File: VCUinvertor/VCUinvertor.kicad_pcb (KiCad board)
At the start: 2 copper layers, 97.3 x 113.8 mm, 96 parts, among them J1 NXP12, J2 NXP11, J3 NXP15, J4 NXP14, J5 NXP10, J6 NXP13, J7 PowerSupply, J8 CAN_NXP, J9 BACKLIGHT, Q1 BSS138, Q10 BSS138, Q2 BSS138, Q3 BSS138, Q4 BSS138, Q5 BSS138, Q6 BSS138, Q7 BSS138, Q8 BSS138, Q9 BSS138, U1 TJA1448ATK, U2 REF3433T, U3 TLV76150DCY

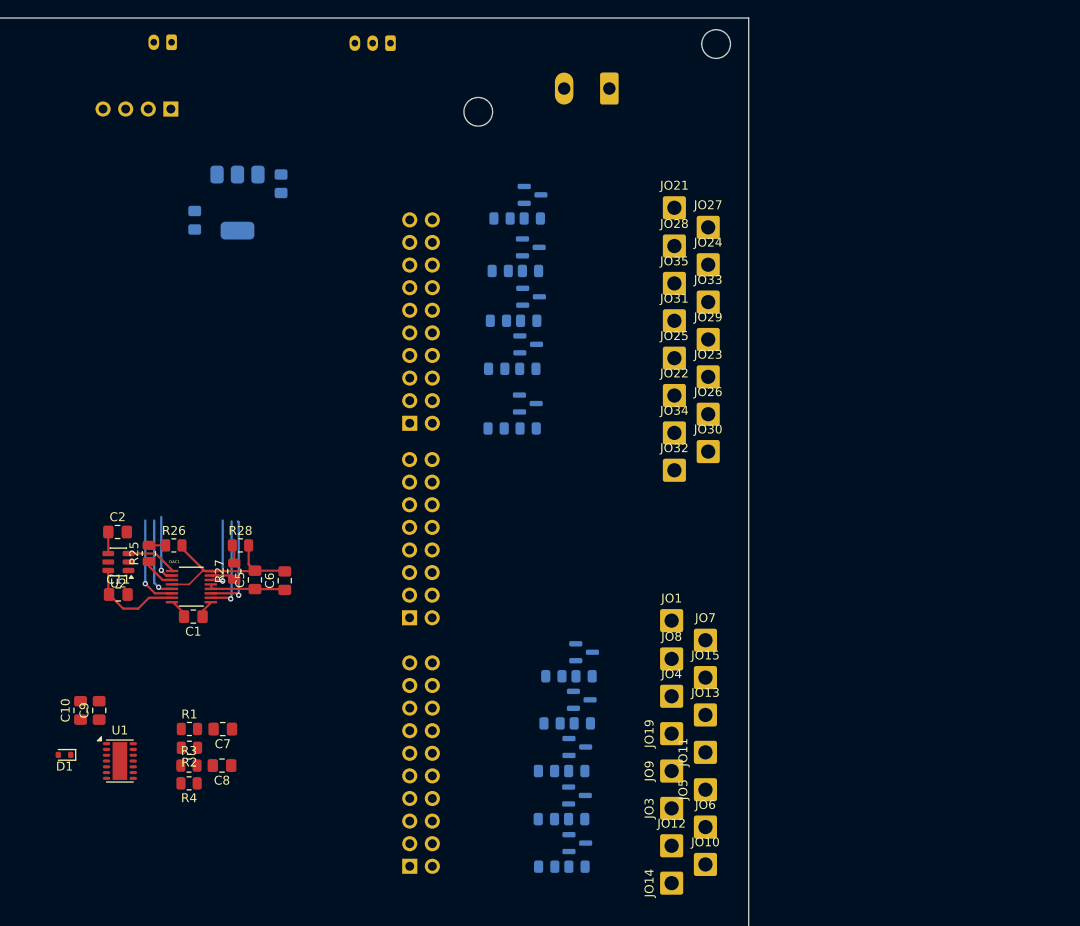
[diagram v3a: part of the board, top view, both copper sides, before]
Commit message: New PMOS config for switching
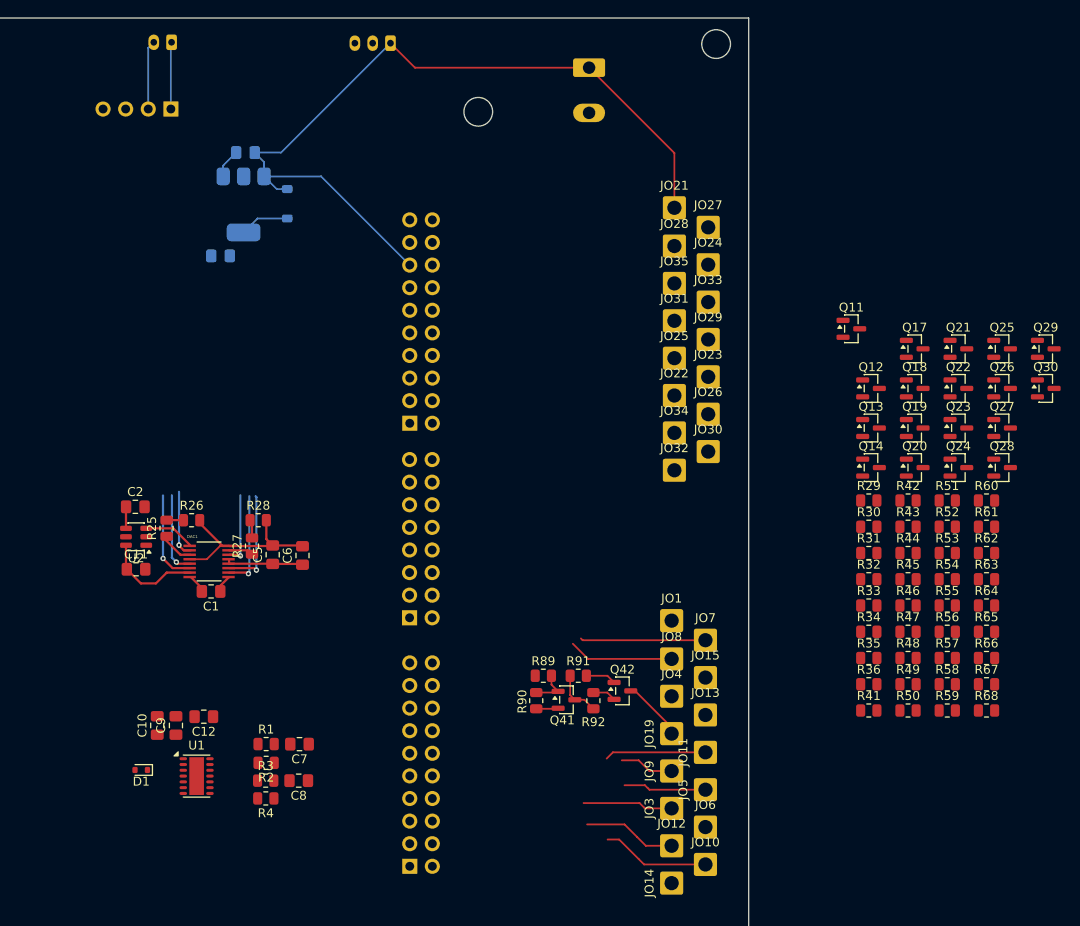
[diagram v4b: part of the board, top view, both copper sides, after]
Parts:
- removed Q1, Q10, Q2, Q3, Q4, Q5, Q6, Q7, Q8, Q9: BSS138, Package_TO_SOT_SMD:SOT-23
- removed R10, R11, R12, R13, R14, R16, R18, R20, R22, R24: 5k, Resistor_SMD:R_0805_2012Metric
- removed R15, R17, R19, R21, R23, R5, R6, R7, R8, R9: 10k, Resistor_SMD:R_0805_2012Metric
- added C12: 0.1uF, Capacitor_SMD:C_0805_2012Metric_Pad1.18x1.45mm_HandSolder, F.Cu at (89.0, 116.3)
- added D1: MBR0540, Diode_SMD:D_SOD-123, B.Cu at (98.4, 58.6)
- added Q11: MMBT3904, Package_TO_SOT_SMD:SOT-23, F.Cu at (161.8, 72.7)
- added Q12: IRLML6402, Package_TO_SOT_SMD:SOT-23, F.Cu at (164.0, 79.4)
- added Q13: MMBT3904, Package_TO_SOT_SMD:SOT-23, F.Cu at (164.0, 83.8)
- added Q14: IRLML6402, Package_TO_SOT_SMD:SOT-23, F.Cu at (164.0, 88.3)
- added Q17: MMBT3904, Package_TO_SOT_SMD:SOT-23, F.Cu at (168.9, 75.0)
- added Q18: MMBT3904, Package_TO_SOT_SMD:SOT-23, F.Cu at (168.9, 79.4)
- added Q19: MMBT3904, Package_TO_SOT_SMD:SOT-23, F.Cu at (168.9, 83.8)
- added Q20: IRLML6402, Package_TO_SOT_SMD:SOT-23, F.Cu at (168.9, 88.3)
- added Q21: IRLML6402, Package_TO_SOT_SMD:SOT-23, F.Cu at (173.8, 75.0)
- added Q22: IRLML6402, Package_TO_SOT_SMD:SOT-23, F.Cu at (173.8, 79.4)
- added Q23: MMBT3904, Package_TO_SOT_SMD:SOT-23, F.Cu at (173.8, 83.8)
- added Q24: IRLML6402, Package_TO_SOT_SMD:SOT-23, F.Cu at (173.8, 88.3)
- added Q25: MMBT3904, Package_TO_SOT_SMD:SOT-23, F.Cu at (178.7, 75.0)
- added Q26: IRLML6402, Package_TO_SOT_SMD:SOT-23, F.Cu at (178.7, 79.4)
- added Q27: MMBT3904, Package_TO_SOT_SMD:SOT-23, F.Cu at (178.7, 83.8)
- added Q28: IRLML6402, Package_TO_SOT_SMD:SOT-23, F.Cu at (178.7, 88.3)
- added Q29: MMBT3904, Package_TO_SOT_SMD:SOT-23, F.Cu at (183.6, 75.0)
- added Q30: IRLML6402, Package_TO_SOT_SMD:SOT-23, F.Cu at (183.6, 79.4)
- added Q41: MMBT3904, Package_TO_SOT_SMD:SOT-23, F.Cu at (129.8, 114.4)
- added Q42: IRLML6402, Package_TO_SOT_SMD:SOT-23, F.Cu at (136.1, 113.4)
- added R29: 10k, Resistor_SMD:R_0805_2012Metric, F.Cu at (163.8, 92.0)
- added R30: 100k, Resistor_SMD:R_0805_2012Metric, F.Cu at (163.8, 95.0)
- added R31: 100, Resistor_SMD:R_0805_2012Metric, F.Cu at (163.8, 97.9)
- added R32: 10k, Resistor_SMD:R_0805_2012Metric, F.Cu at (163.8, 100.8)
- added R33: 10k, Resistor_SMD:R_0805_2012Metric, F.Cu at (163.8, 103.8)
- added R34: 100k, Resistor_SMD:R_0805_2012Metric, F.Cu at (163.8, 106.8)
- added R35: 100, Resistor_SMD:R_0805_2012Metric, F.Cu at (163.8, 109.7)
- added R36: 10k, Resistor_SMD:R_0805_2012Metric, F.Cu at (163.8, 112.7)
- added R41: 10k, Resistor_SMD:R_0805_2012Metric, F.Cu at (163.8, 115.6)
- added R42: 100k, Resistor_SMD:R_0805_2012Metric, F.Cu at (168.2, 92.0)
- added R43: 10k, Resistor_SMD:R_0805_2012Metric, F.Cu at (168.2, 95.0)
- added R44: 100k, Resistor_SMD:R_0805_2012Metric, F.Cu at (168.2, 97.9)
- added R45: 10k, Resistor_SMD:R_0805_2012Metric, F.Cu at (168.2, 100.8)
- added R46: 100k, Resistor_SMD:R_0805_2012Metric, F.Cu at (168.2, 103.8)
- added R47: 100, Resistor_SMD:R_0805_2012Metric, F.Cu at (168.2, 106.8)
- added R48: 100, Resistor_SMD:R_0805_2012Metric, F.Cu at (168.2, 109.7)
- added R49: 100, Resistor_SMD:R_0805_2012Metric, F.Cu at (168.2, 112.7)
- added R50: 10k, Resistor_SMD:R_0805_2012Metric, F.Cu at (168.2, 115.6)
- added R51: 10k, Resistor_SMD:R_0805_2012Metric, F.Cu at (172.6, 92.0)
- added R52: 10k, Resistor_SMD:R_0805_2012Metric, F.Cu at (172.6, 95.0)
- added R53: 10k, Resistor_SMD:R_0805_2012Metric, F.Cu at (172.6, 97.9)
- added R54: 100k, Resistor_SMD:R_0805_2012Metric, F.Cu at (172.6, 100.8)
- added R55: 100, Resistor_SMD:R_0805_2012Metric, F.Cu at (172.6, 103.8)
- added R56: 10k, Resistor_SMD:R_0805_2012Metric, F.Cu at (172.6, 106.8)
- added R57: 10k, Resistor_SMD:R_0805_2012Metric, F.Cu at (172.6, 109.7)
- added R58: 100k, Resistor_SMD:R_0805_2012Metric, F.Cu at (172.6, 112.7)
- added R59: 100, Resistor_SMD:R_0805_2012Metric, F.Cu at (172.6, 115.6)
- added R60: 10k, Resistor_SMD:R_0805_2012Metric, F.Cu at (177.0, 92.0)
- added R61: 10k, Resistor_SMD:R_0805_2012Metric, F.Cu at (177.0, 95.0)
- added R62: 100k, Resistor_SMD:R_0805_2012Metric, F.Cu at (177.0, 97.9)
- added R63: 100, Resistor_SMD:R_0805_2012Metric, F.Cu at (177.0, 100.8)
- added R64: 10k, Resistor_SMD:R_0805_2012Metric, F.Cu at (177.0, 103.8)
- added R65: 10k, Resistor_SMD:R_0805_2012Metric, F.Cu at (177.0, 106.8)
- added R66: 100k, Resistor_SMD:R_0805_2012Metric, F.Cu at (177.0, 109.7)
- added R67: 100, Resistor_SMD:R_0805_2012Metric, F.Cu at (177.0, 112.7)
- added R68: 10k, Resistor_SMD:R_0805_2012Metric, F.Cu at (177.0, 115.6)
- added R89: 10k, Resistor_SMD:R_0805_2012Metric, F.Cu at (127.2, 111.7)
- added R90: 100k, Resistor_SMD:R_0805_2012Metric, F.Cu at (126.4, 114.5)
- added R91: 100, Resistor_SMD:R_0805_2012Metric, F.Cu at (131.1, 111.7)
- added R92: 10k, Resistor_SMD:R_0805_2012Metric, F.Cu at (132.8, 114.5)
- moved C10 8.79 mm to (83.8, 117.3)
- moved C8 8.79 mm to (99.7, 123.5)
- moved C9 8.79 mm to (85.9, 117.3)
- moved R1 8.79 mm to (96.0, 119.4)
- moved R2 8.79 mm to (96.0, 121.5)
- moved R3 8.79 mm to (96.0, 123.5)
- moved U1 8.79 mm to (88.2, 123.0)
- moved C7 8.79 mm to (99.8, 119.4)
- moved D1 8.79 mm to (82.0, 122.3)
- moved R4 8.79 mm to (96.0, 125.5)
- moved C3 5.32 mm to (93.7, 52.9), turned to 180 degrees
- moved C4 4.94 mm to (90.9, 64.5), turned to 180 degrees
- moved C1 3.46 mm to (89.8, 102.2)
- moved C2 3.46 mm to (81.3, 92.7)
- moved C5 3.46 mm to (96.8, 98.1)
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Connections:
- C10 pad 1: Net-(D1-K) -> +5V
- C9 pad 1: Net-(D1-K) -> +5V
- J3 pad 1: unconnected-(J3-Pin_1-Pad1) -> /Pzz
- U1 pad 11: /Pyy -> +3.3V
- U1 pad 14: /Pxx -> /Pyy
- U1 pad 15: unconnected-(U1-GND-Pad15) -> (no net)
- U1 pad 3: Net-(D1-K) -> +5V
- U1 pad 5: /TX1 -> GND
- U1 pad 6: GND -> /TX1
- U1 pad 7: unconnected-(U1-NC-Pad7) -> /RX1
- U1 pad 8: /RX1 -> /Pzz
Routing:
- net +12V: track 0.00 -> 93.0 mm
- net /CANL01: track 0.00 -> 14.1 mm
- net /Brk_AN1: track 7.60 -> 19.8 mm
- net /CANH01: track 0.00 -> 11.8 mm
- net /ECO1: track 0.00 -> 11.4 mm
- net NXP_TPS01: track 3.88 -> 14.4 mm
- net /REV1: track 0.00 -> 10.1 mm
- net /FWD1: track 0.00 -> 9.31 mm
- net /CAN_L: track 0.00 -> 7.76 mm
- net /CAN_H: track 0.00 -> 7.53 mm
- net /ACC1: track 0.00 -> 6.99 mm
- net /H_Brk1: track 0.00 -> 6.10 mm
- net GND: track 23.3 -> 29.0 mm
- net +5V: track 17.1 -> 22.6 mm
- net Net-(Q41-C): track 0.00 -> 5.42 mm
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
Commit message: VCU_PinCorrection_0.1
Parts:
- removed the D1 at (82.0, 122.3)
- moved Q21 79.2 mm to (174.3, 154.1)
- moved Q27 71.0 mm to (127.7, 133.2)
- moved R61 66.6 mm to (122.0, 132.5)
- moved Q28 64.3 mm to (133.6, 134.1)
- moved Q23 63.5 mm to (128.1, 127.9)
- moved R62 63.1 mm to (124.7, 133.3), turned to -90 degrees
- moved R51 62.1 mm to (171.4, 154.1), turned to 90 degrees
- moved R41 59.4 mm to (125.1, 70.5)
- moved R53 58.2 mm to (122.4, 127.3)
- moved Q11 57.1 mm to (127.0, 118.0)
- moved Q24 55.9 mm to (134.4, 127.9)
- moved R63 55.6 mm to (130.6, 131.6)
- moved R64 55.6 mm to (130.6, 134.4), turned to 90 degrees
- moved R50 55.4 mm to (133.7, 72.2), turned to 90 degrees
- moved R54 54.7 mm to (125.1, 128.0), turned to -90 degrees
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- renumbered J5 to NXP10, J2 to NXP11, J1 to NXP12, J6 to NXP13, J4 to NXP14, J3 to NXP15
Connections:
- DAC1 pad 14: /Brk_AN2 -> /Brk_AN1
- DAC1 pad 15: NXP_TPS02 -> NXP_TPS01
- DAC1 pad 2: /Brk_AN1 -> /Brk_AN2
- DAC1 pad 3: NXP_TPS01 -> NXP_TPS02
- J9 pad 2: BACKLIGHT_ON -> BREAKLIGHT
- NXP10 pad 13: unconnected-(J5-Pin_13-Pad13) -> /RX1
- NXP10 pad 15: unconnected-(J5-Pin_15-Pad15) -> /TX1
- NXP10 pad 2: unconnected-(J5-Pin_2-Pad2) -> /TX0
- NXP10 pad 4: unconnected-(J5-Pin_4-Pad4) -> /RX0
- NXP13 pad 10: /NXP_REV02 -> unconnected-(NXP13-Pin_10-Pad10)
- NXP13 pad 2: /NXP_ACC02 -> unconnected-(NXP13-Pin_2-Pad2)
- NXP13 pad 4: /NXP_ECO02 -> unconnected-(NXP13-Pin_4-Pad4)
- NXP13 pad 6: /NXP_BRK02 -> unconnected-(NXP13-Pin_6-Pad6)
- NXP13 pad 8: /NXP_FWD02 -> unconnected-(NXP13-Pin_8-Pad8)
- NXP14 pad 1: unconnected-(J4-Pin_1-Pad1) -> NXP_TPSOUT01
- NXP14 pad 10: /NXP_ACC01 -> unconnected-(NXP14-Pin_10-Pad10)
- NXP14 pad 12: /NXP_ECO01 -> unconnected-(NXP14-Pin_12-Pad12)
- NXP14 pad 14: /NXP_BRK01 -> unconnected-(NXP14-Pin_14-Pad14)
- NXP14 pad 16: /NXP_FWD01 -> unconnected-(NXP14-Pin_16-Pad16)
- NXP14 pad 18: /NXP_REV01 -> unconnected-(NXP14-Pin_18-Pad18)
- NXP14 pad 2: /PWM_NXP4 -> unconnected-(NXP14-Pin_2-Pad2)
- NXP14 pad 20: BACKLIGHT_ON -> unconnected-(NXP14-Pin_20-Pad20)
- NXP14 pad 3: unconnected-(J4-Pin_3-Pad3) -> NXP_TPSOUT02
- NXP14 pad 4: /PWM_NXP3 -> unconnected-(NXP14-Pin_4-Pad4)
- NXP14 pad 6: /PWM_NXP2 -> unconnected-(NXP14-Pin_6-Pad6)
- NXP14 pad 8: /PWM_NXP1 -> unconnected-(NXP14-Pin_8-Pad8)
- NXP15 pad 1: /Pzz -> unconnected-(NXP15-Pin_1-Pad1)
- NXP15 pad 10: /TX1 -> unconnected-(NXP15-Pin_10-Pad10)
- NXP15 pad 12: /RX1 -> unconnected-(NXP15-Pin_12-Pad12)
- NXP15 pad 18: NXP_TPSOUT01 -> unconnected-(NXP15-Pin_18-Pad18)
- NXP15 pad 2: /Pxx -> unconnected-(NXP15-Pin_2-Pad2)
- NXP15 pad 20: NXP_TPSOUT02 -> unconnected-(NXP15-Pin_20-Pad20)
- NXP15 pad 4: /Pyy -> unconnected-(NXP15-Pin_4-Pad4)
- NXP15 pad 6: /TX0 -> unconnected-(NXP15-Pin_6-Pad6)
- NXP15 pad 8: /RX0 -> unconnected-(NXP15-Pin_8-Pad8)
- R1 pad 1: /CANH01 -> /CANH02
- R2 pad 2: /CANL01 -> /CANL02
- R3 pad 1: /CANH02 -> /CANH01
- R4 pad 2: /CANL02 -> /CANL01
- U1 pad 10: /CANH02 -> /CANH01
- U1 pad 12: /CANL01 -> /CANL02
- U1 pad 13: /CANH01 -> /CANH02
- U1 pad 9: /CANL02 -> /CANL01
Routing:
- net NXP_TPS02: track 2.75 -> 51.6 mm, vias 0 -> 1
- net NXP_TPS01: track 14.4 -> 52.6 mm, vias 0 -> 1
- net /Brk_AN2: track 8.13 -> 45.1 mm
- net /Brk_AN1: track 19.8 -> 48.0 mm
- net /CANL02: track 0.00 -> 22.1 mm
- net /CANH02: track 0.00 -> 17.0 mm
- net GND: track 29.0 -> 46.0 mm
- net +12V: track 93.0 -> 108.3 mm, vias 0 -> 5
- net +5V: track 22.6 -> 37.6 mm
- net /CANH01: track 11.8 -> 22.3 mm
- net /Pzz: track 0.00 -> 9.07 mm
- net /PWM_NXP4: track 11.0 -> 2.37 mm
- net /PWM_NXP3: track 11.5 -> 3.16 mm
- net /PWM_NXP2: track 9.41 -> 1.70 mm
- net /PWM_NXP1: track 10.7 -> 3.57 mm
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- added copper zone on B.Cu, net +12V
- added copper zone on F.Cu, net GND

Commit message: Pin_Assignment_Main_Done
[15:48, 3/30/2026] Viorel VCU: ptb22 - j12 - pin 1 - LPUART1_TX - UART_INV01 pin 3
ptb23 - j12 - pin 3 - LPUART1_RX - UART_INV01 pin 2
ptd2 - j11 - pin 5 - LPUART3_TX - UART_INV02 pin 3
ptd3 - j11 - pin 7 - LPUART3_RX - UART_INV01 pin 2
[15:55, 3/30/2026] Viorel VCU: pte23 - j15 - pin 9 - EMIOS1_CH3_H - PWM_NXP1
pte24 - j15 - pin 11 - EMIOS1_CH4_H - PWM_NXP2
pte25 - j15 - pin 13 - EMIOS1_CH5_H - PWM_NXP3
pte26 - j15 - pin 15 - EMIOS1_CH6_H - PWM_NXP4
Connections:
- JU1 pad 1: /V+ -> /V+1
- JU1 pad 2: /Tx -> /Tx_UART01
- JU1 pad 3: /Rx -> /Rx_UART01
- JU1 pad 4: /V- -> /V-1
- JU2 pad 1: /V+ -> /V+2
- JU2 pad 2: /Tx -> /Tx_UART02
- JU2 pad 3: /Rx -> /Rx_UART02
- JU2 pad 4: /V- -> /V-2
- NXP11 pad 2: unconnected-(NXP11-Pin_2-Pad2) -> /Rx_UART02
- NXP11 pad 3: unconnected-(NXP11-Pin_3-Pad3) -> /Tx_UART02
- NXP12 pad 2: unconnected-(NXP12-Pin_2-Pad2) -> /Rx_UART01
- NXP12 pad 3: unconnected-(NXP12-Pin_3-Pad3) -> /Tx_UART01
- NXP15 pad 11: unconnected-(NXP15-Pin_11-Pad11) -> /PWM_NXP2
- NXP15 pad 13: unconnected-(NXP15-Pin_13-Pad13) -> /PWM_NXP3
- NXP15 pad 15: unconnected-(NXP15-Pin_15-Pad15) -> /PWM_NXP4
- NXP15 pad 9: unconnected-(NXP15-Pin_9-Pad9) -> /PWM_NXP1

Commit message: FirstLayout_Completed
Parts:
- removed Q11, Q13, Q17, Q18, Q19, Q23, Q25, Q27, Q29, Q41: MMBT3904, Package_TO_SOT_SMD:SOT-23
- removed Q12, Q14, Q20, Q21, Q22, Q24, Q26, Q28, Q30, Q42: IRLML6402, Package_TO_SOT_SMD:SOT-23
- removed R29, R32, R33, R36, R41, R43, R45, R50, R51, R52, R53, R56, R57, R60, R61, R65, R68, R89, R92: 10k, Resistor_SMD:R_0805_2012Metric
- removed R30, R34, R42, R44, R46, R54, R58, R62, R66, R90: 100k, Resistor_SMD:R_0805_2012Metric
- removed R31, R35, R47, R48, R49, R55, R59, R67, R91: 100, Resistor_SMD:R_0805_2012Metric
- added Q1: 2N7002, Package_TO_SOT_SMD:SOT-23, F.Cu at (130.8, 68.8)
- added Q10: 2N7002, Package_TO_SOT_SMD:SOT-23, F.Cu at (130.8, 83.4)
- added Q2: 2N7002, Package_TO_SOT_SMD:SOT-23, F.Cu at (130.8, 114.5)
- added Q3: 2N7002, Package_TO_SOT_SMD:SOT-23, F.Cu at (130.8, 118.2)
- added Q4: 2N7002, Package_TO_SOT_SMD:SOT-23, F.Cu at (130.8, 122.0)
- added Q5: 2N7002, Package_TO_SOT_SMD:SOT-23, F.Cu at (130.8, 125.5)
- added Q6: 2N7002, Package_TO_SOT_SMD:SOT-23, F.Cu at (130.8, 129.2)
- added Q7: 2N7002, Package_TO_SOT_SMD:SOT-23, F.Cu at (130.8, 72.5)
- added Q8: 2N7002, Package_TO_SOT_SMD:SOT-23, F.Cu at (130.8, 76.1)
- added Q9: 2N7002, Package_TO_SOT_SMD:SOT-23, F.Cu at (130.8, 79.8)
- added R10: 10k, Resistor_SMD:R_0805_2012Metric, F.Cu at (134.8, 121.8)
- added R11: 10k, Resistor_SMD:R_0805_2012Metric, F.Cu at (126.8, 124.5)
- added R12: 10k, Resistor_SMD:R_0805_2012Metric, F.Cu at (134.8, 125.5)
- added R13: 10k, Resistor_SMD:R_0805_2012Metric, F.Cu at (126.8, 128.2)
- added R14: 10k, Resistor_SMD:R_0805_2012Metric, F.Cu at (134.8, 129.2)
- added R15: 10k, Resistor_SMD:R_0805_2012Metric, F.Cu at (126.8, 71.9)
- added R16: 10k, Resistor_SMD:R_0805_2012Metric, F.Cu at (134.8, 72.5)
- added R17: 10k, Resistor_SMD:R_0805_2012Metric, F.Cu at (126.8, 75.4)
- added R18: 10k, Resistor_SMD:R_0805_2012Metric, F.Cu at (134.8, 76.2)
- added R19: 10k, Resistor_SMD:R_0805_2012Metric, F.Cu at (126.8, 78.8)
- added R20: 10k, Resistor_SMD:R_0805_2012Metric, F.Cu at (134.8, 79.8)
- added R21: 10k, Resistor_SMD:R_0805_2012Metric, F.Cu at (126.8, 82.2)
- added R22: 10k, Resistor_SMD:R_0805_2012Metric, F.Cu at (134.8, 83.5)
- added R5: 10k, Resistor_SMD:R_0805_2012Metric, F.Cu at (126.8, 113.5)
- added R6: 10k, Resistor_SMD:R_0805_2012Metric, F.Cu at (134.8, 114.5)
- added R7: 10k, Resistor_SMD:R_0805_2012Metric, F.Cu at (126.8, 117.2)
- added R8: 10k, Resistor_SMD:R_0805_2012Metric, F.Cu at (134.8, 118.2)
- added R9: 10k, Resistor_SMD:R_0805_2012Metric, F.Cu at (126.8, 120.8)
- NXP10, NXP12: footprint Connector_PinHeader_2.54mm:PinHeader_2x08_P2.54mm_Vertical -> Connector_PinHeader_2.54mm:PinHeader_2x10_P2.54mm_Vertical
- NXP13, NXP14: footprint Connector_PinHeader_2.54mm:PinHeader_2x10_P2.54mm_Vertical -> Connector_PinHeader_2.54mm:PinHeader_2x08_P2.54mm_Vertical
- R63: value 100 -> 10k
- moved NXP12 79.8 mm to (112.2, 133.1), turned to 0 degrees
- moved R64 65.7 mm to (134.8, 68.9), turned to 180 degrees
- moved R63 63.2 mm to (126.8, 68.5)
- moved NXP14 63.1 mm to (63.9, 92.5), turned to 180 degrees
- moved NXP13 50.2 mm to (63.9, 69.6), turned to 180 degrees
- moved NXP11 49.9 mm to (112.2, 105.2), turned to 0 degrees
- moved J9 37.7 mm to (72.3, 40.9)
- moved NXP10 21.9 mm to (112.2, 83.3)
- moved JU1 17.3 mm to (112.5, 148.1)
- moved JU2 17.3 mm to (99.9, 148.3)
- moved R28 12.6 mm to (96.1, 92.5)
- moved C4 11.1 mm to (101.8, 66.4)
- moved R25 10.5 mm to (101.3, 101.7), turned to -90 degrees
- moved R27 9.74 mm to (98.8, 91.8), turned to 180 degrees
- moved C3 8.99 mm to (102.5, 54.8)
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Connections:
- JU1 pad 1: /V+1 -> unconnected-(JU1-Pin_1-Pad1)
- JU1 pad 4: /V-1 -> GND
- JU2 pad 1: /V+2 -> unconnected-(JU2-Pin_1-Pad1)
- JU2 pad 4: /V-2 -> GND
- NXP10 pad 10: unconnected-(NXP10-Pin_10-Pad10) -> /NXP_BRK02
- NXP10 pad 12: unconnected-(NXP10-Pin_12-Pad12) -> /NXP_ECO02
- NXP10 pad 14: unconnected-(NXP10-Pin_14-Pad14) -> /NXP_ACC02
- NXP10 pad 6: unconnected-(NXP10-Pin_6-Pad6) -> /NXP_REV02
- NXP10 pad 8: unconnected-(NXP10-Pin_8-Pad8) -> /NXP_FWD02
- NXP12 pad 2: /Rx_UART01 -> /NXP_REV01
- NXP12 pad 3: /Tx_UART01 -> unconnected-(NXP12-Pin_3-Pad3)
- NXP12 pad 4: unconnected-(NXP12-Pin_4-Pad4) -> /NXP_FWD01
- NXP12 pad 5: unconnected-(NXP12-Pin_5-Pad5) -> /NXP_BRK01
- NXP12 pad 6: unconnected-(NXP12-Pin_6-Pad6) -> /Tx_UART01
- NXP12 pad 8: unconnected-(NXP12-Pin_8-Pad8) -> /Rx_UART01
- NXP13 pad 1: unconnected-(NXP13-Pin_1-Pad1) -> +12V
- NXP13 pad 15: +12V -> unconnected-(NXP13-Pin_15-Pad15)
- NXP13 pad 2: unconnected-(NXP13-Pin_2-Pad2) -> BREAKLIGHT
- R63 pad 1: Net-(Q27-C) -> /NXP_ACC02
- R64 pad 2: Net-(Q27-C) -> /ACC2
- U1 pad 15: (no net) -> GND
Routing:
- net +12V: track 108.3 -> 269.5 mm, vias 5 -> 10
- net +5V: track 37.6 -> 90.7 mm, vias 0 -> 3
- net /PWM_NXP2: track 1.70 -> 50.5 mm, vias 1 -> 0
- net /Tx_UART02: track 0.00 -> 48.6 mm, vias 0 -> 1
- net /PWM_NXP4: track 2.37 -> 50.4 mm, vias 1 -> 0
- net /PWM_NXP3: track 3.16 -> 51.2 mm, vias 1 -> 2
- net /Rx_UART02: track 0.00 -> 47.7 mm
- net +3.3V: track 14.5 -> 60.0 mm, vias 0 -> 4
- net /PWM_NXP1: track 3.57 -> 48.9 mm, vias 1 -> 0
- net NXP_TPSOUT01: track 1.91 -> 44.4 mm, vias 0 -> 1
- net /TX1: track 4.37 -> 46.6 mm, vias 0 -> 1
- net /RX1: track 3.90 -> 45.7 mm, vias 0 -> 1
- net NXP_TPSOUT02: track 2.08 -> 35.5 mm
- net BREAKLIGHT: track 0.00 -> 32.5 mm
- net /Rx_UART01: track 0.00 -> 24.1 mm
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- added copper zone on B.Cu, net GND
- removed copper zone on B.Cu, net +12V
- removed copper zone on F.Cu, net GND
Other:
- outline, holes or cut-outs redrawn
- board text added: "Board size: 114mm x 97mm"
